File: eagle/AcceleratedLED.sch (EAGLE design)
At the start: 19 parts, among them Q1 16MHZ, U1 ATMEGA328, U8 TXB0108PWR

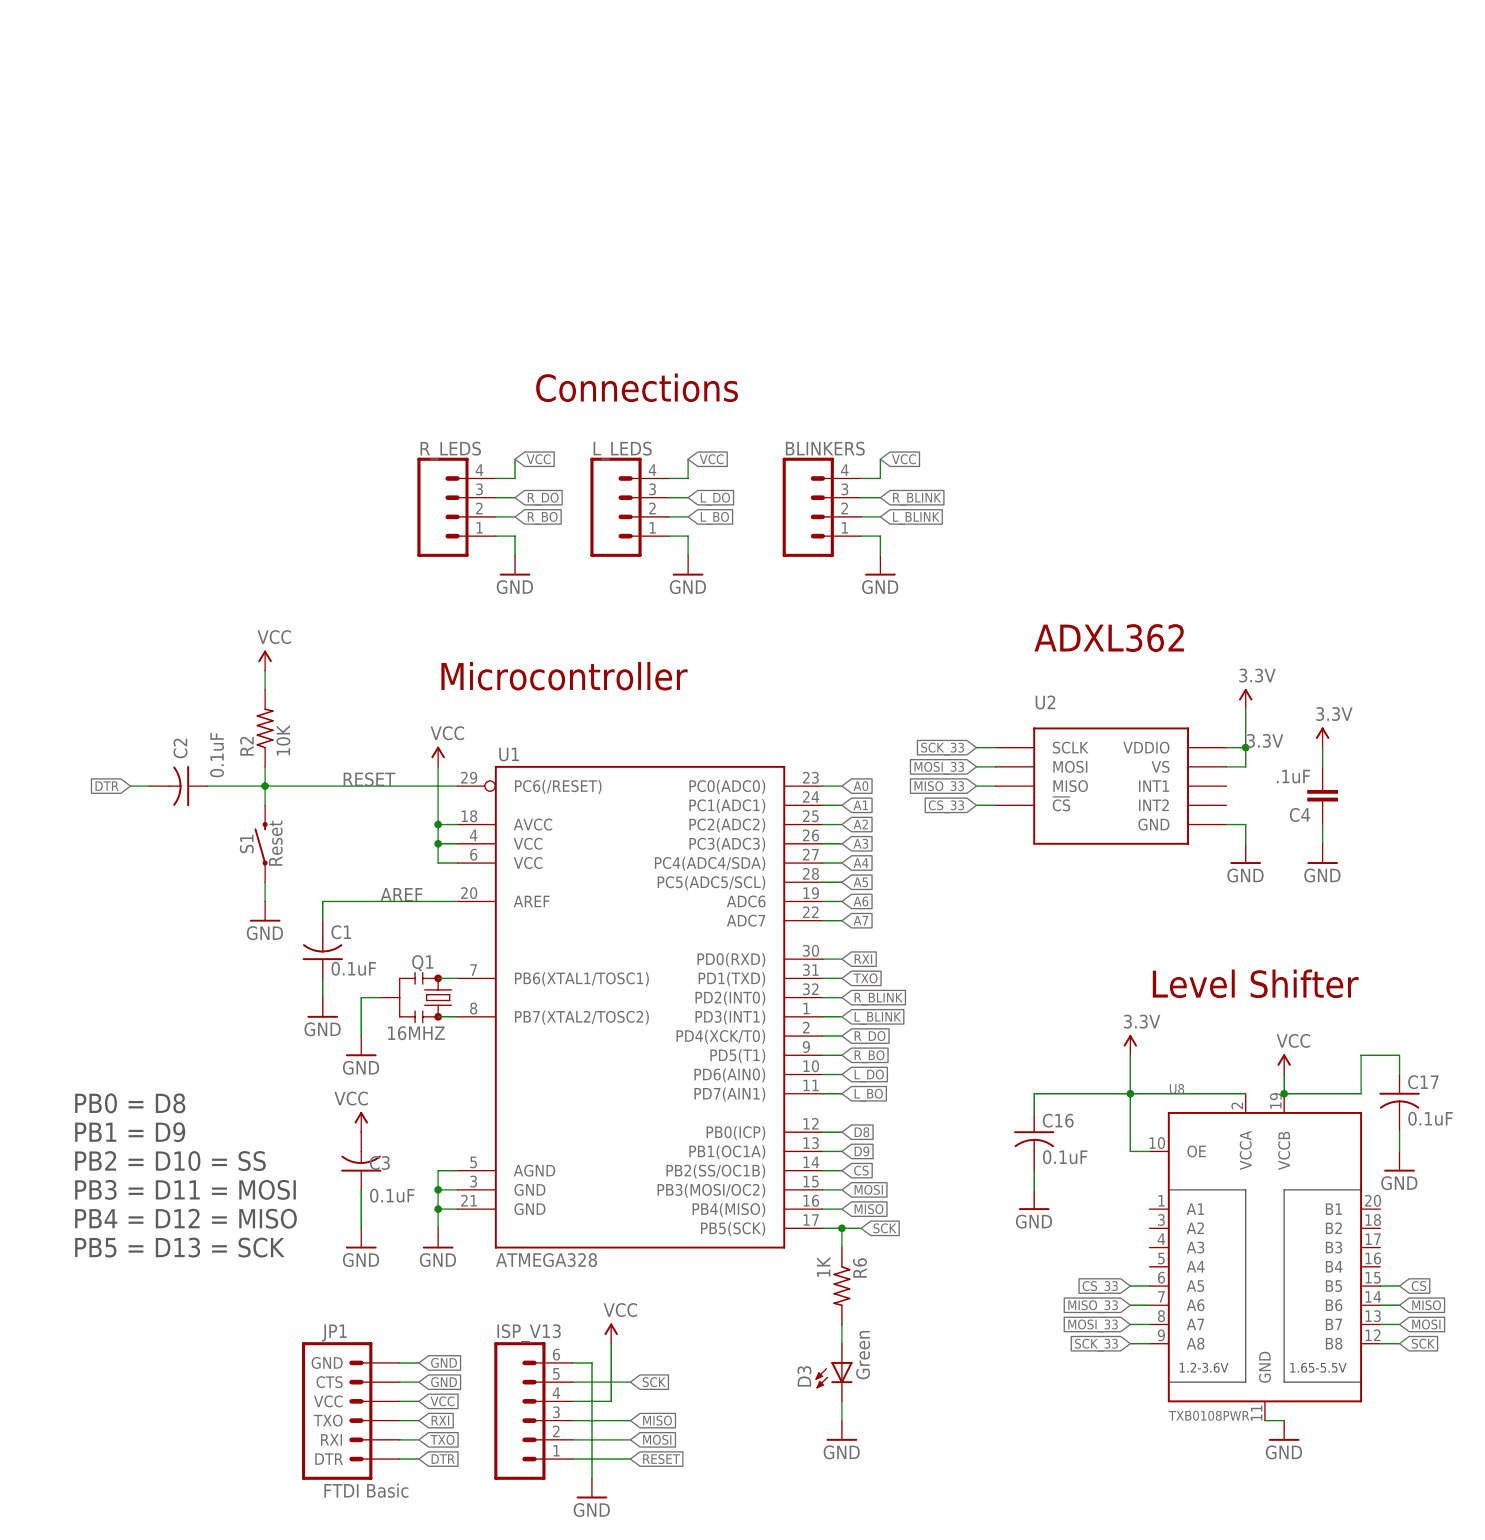
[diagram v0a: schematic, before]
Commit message: Add switching power
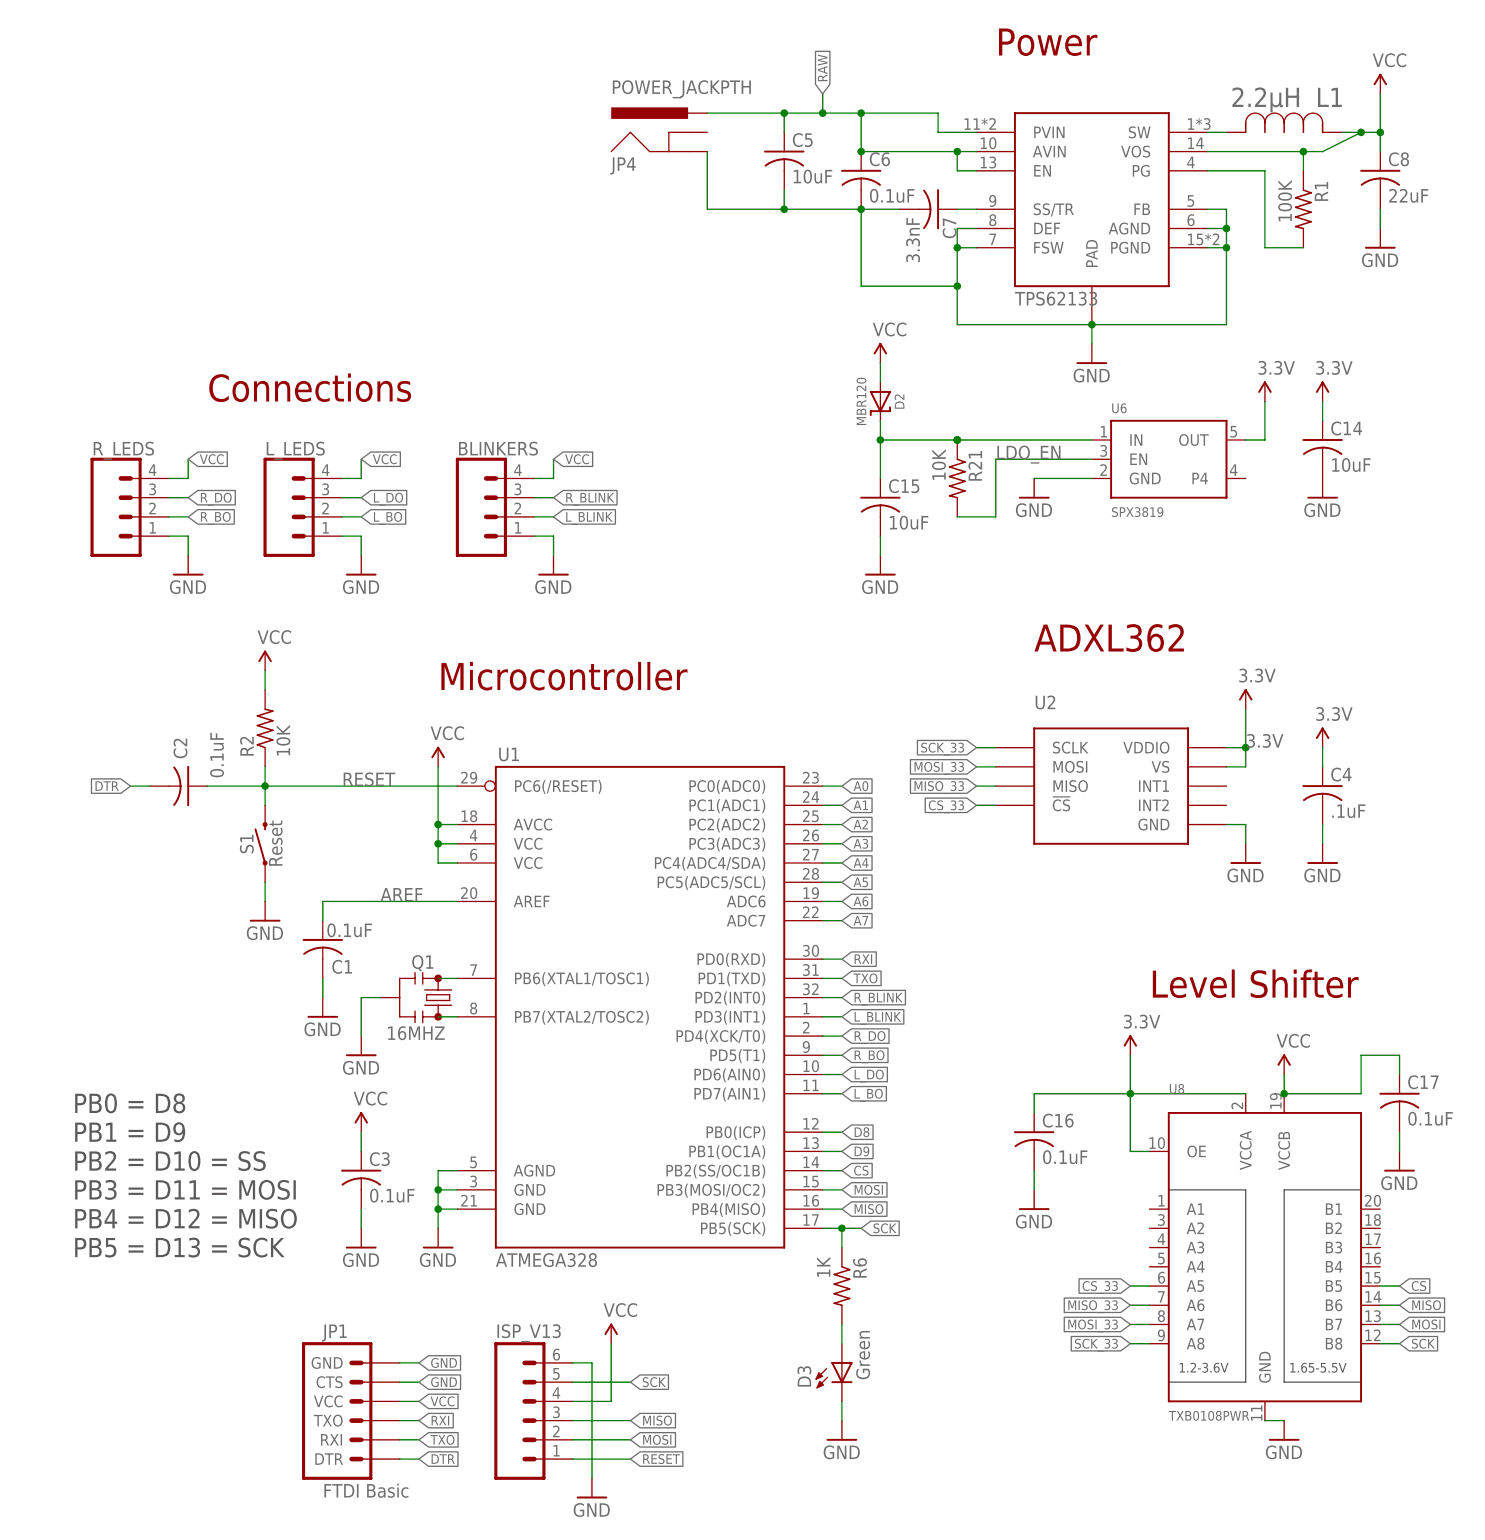
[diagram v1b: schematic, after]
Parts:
- added C14, C5: 10uF, RemoteMotion:C-USC0805
- added C15: 10uF, MotionSign:C-USC0805
- added C6: 0.1uF, MotionSign:C-USC0805
- added C7: 3.3nF, MotionSign:C-USC0805
- added C8: 22uF, RemoteMotion:C-USC0805
- added D2: MBR120, MotionSign:DIODE-SCHOTTKYSOD-123
- added IC1: TPS62133, robopoly:TPS62133
- added JP4: POWER_JACKPTH, MotionSign:POWER_JACKPTH
- added L1: 2.2μH, bg_eagle_lib:IHLP1212BZER2R2M11IND_IHLP-1212BZ-L
- added R1: 100K, MotionSign:R-US_M0805
- added R21: 10K, MotionSign:R-US_M0805
- added U6: SPX3819, MotionSign:VREG_SOT23-5
- C4: device SparkFun-Capacitors:0.1UF-25V(+80/-20%)(0603) -> RemoteMotion:C-USC0805; PROD_ID CAP-00810 -> (none)
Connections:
- new net LDO_EN: R21.2, U6.EN
- new net N$23: C15.1, D2.C, R21.1, U6.IN
- new net PG: IC1.PG, R1.2
- new net RAW: C5.1, C6.1, IC1.AVIN, IC1.EN, IC1.PVIN, JP4.PWR
- new net SS/TR: C7.1, IC1.SS/TR
- new net SW: IC1.SW, L1.2
- net 3.3V: now also C14.1, C4.1, U6.OUT; no longer C4.2
- net AREF: now also C1.1; no longer C1.2
- net GND: now also C1.2, C14.2, C15.2, C3.2, C4.2, C5.2, C6.2, C7.2, C8.2, IC1.AGND, IC1.DEF, IC1.FB, IC1.FSW, IC1.PAD, IC1.PGND, JP4.GND, U6.GND; no longer C1.1, C3.1, C4.1
- net VCC: now also C3.1, C8.1, D2.A, IC1.VOS, L1.1, R1.1; no longer C3.2
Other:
- note added: "Power"
- moved on the sheet: BLINKERS, C1, C3, L_LEDS, R_LEDS

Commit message: changes
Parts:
- BLINKERS: device MotionSign:CONN_04JST-PTH -> SparkFun-Connectors:M03JST-PTH
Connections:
- net L_BO renamed L_SCK
- net L_DO renamed L_DATA
- net R_BO renamed R_SCK
- net R_DO renamed R_DATA
- net VCC: no longer BLINKERS.4
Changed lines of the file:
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@@
 <setting verticaltext="up"/>
 </settings>
-<grid distance="0.1" unitdist="inch" unit="inch" style="lines" multiple="1" display="yes" altdistance="0.01" altunitdist="inch" altunit="inch"/>
+<grid distance="0.1" unitdist="inch" unit="inch" style="lines" multiple="1" display="no" altdistance="0.01" altunitdist="inch" altunit="inch"/>
 <layers>
 <layer number="1" name="Top" color="4" fill="1" visible="no" active="no"/>
@@
 <part name="L_LEDS" library="MotionSign" library_urn="urn:adsk.eagle:library:3048452" deviceset="CONN_04" device="JST-PTH" package3d_urn="urn:adsk.eagle:package:3048844/2"/>
 <part name="GND9" library="MotionSign" library_urn="urn:adsk.eagle:library:3048452" deviceset="GND" device=""/>
-<part name="BLINKERS" library="MotionSign" library_urn="urn:adsk.eagle:library:3048452" deviceset="CONN_04" device="JST-PTH" package3d_urn="urn:adsk.eagle:package:3048844/2"/>
 <part name="GND10" library="MotionSign" library_urn="urn:adsk.eagle:library:3048452" deviceset="GND" device=""/>
 <part name="C14" library="RemoteMotion" library_urn="urn:adsk.eagle:library:2810894" deviceset="C-US" device="C0805" package3d_urn="urn:adsk.eagle:package:2811338/2" value="10uF"/>
@@
 <part name="JP4" library="MotionSign" library_urn="urn:adsk.eagle:library:3048452" deviceset="POWER_JACK" device="PTH" package3d_urn="urn:adsk.eagle:package:3048907/2" value="POWER_JACKPTH"/>
 <part name="SUPPLY3" library="MotionSign" library_urn="urn:adsk.eagle:library:3048452" deviceset="VCC" device=""/>
+<part name="BLINKERS" library="SparkFun-Connectors" deviceset="M03" device="JST-PTH"/>
 </parts>
 <sheets>
@@
 <instance part="L_LEDS" gate="G$1" x="-15.24" y="129.54"/>
 <instance part="GND9" gate="1" x="-7.62" y="121.92"/>
-<instance part="BLINKERS" gate="G$1" x="10.16" y="129.54"/>
-<instance part="GND10" gate="1" x="17.78" y="121.92"/>
+<instance part="GND10" gate="1" x="17.78" y="149.86"/>
 <instance part="C14" gate="G$1" x="119.38" y="139.7"/>
 <instance part="U6" gate="G$1" x="99.06" y="137.16"/>
@@
 <instance part="JP4" gate="G$1" x="35.56" y="175.26"/>
 <instance part="SUPPLY3" gate="1" x="-7.62" y="48.26"/>
+<instance part="BLINKERS" gate="G$1" x="7.62" y="157.48"/>
 </instances>
 <busses>
@@
 <wire x1="-7.62" y1="127" x2="-7.62" y2="124.46" width="0.1524" layer="91"/>
 <pinref part="GND9" gate="1" pin="GND"/>
-</segment>
-<segment>
-<pinref part="BLINKERS" gate="G$1" pin="1"/>
-<wire x1="15.24" y1="127" x2="17.78" y2="127" width="0.1524" layer="91"/>
-<wire x1="17.78" y1="127" x2="17.78" y2="124.46" width="0.1524" layer="91"/>
-<pinref part="GND10" gate="1" pin="GND"/>
 </segment>
 <segment>
@@
 <wire x1="127" y1="167.64" x2="127" y2="170.18" width="0.1524" layer="91"/>
 </segment>
+<segment>
+<pinref part="BLINKERS" gate="G$1" pin="1"/>
+<wire x1="15.24" y1="154.94" x2="17.78" y2="154.94" width="0.1524" layer="91"/>
+<pinref part="GND10" gate="1" pin="GND"/>
+<wire x1="17.78" y1="152.4" x2="17.78" y2="154.94" width="0.1524" layer="91"/>
+</segment>
 </net>
 <net name="AREF" class="0">
@@
 <wire x1="-7.62" y1="134.62" x2="-7.62" y2="137.16" width="0.1524" layer="91"/>
 <label x="-7.62" y="137.16" size="1.27" layer="95" xref="yes"/>
-</segment>
-<segment>
-<pinref part="BLINKERS" gate="G$1" pin="4"/>
-<wire x1="15.24" y1="134.62" x2="17.78" y2="134.62" width="0.1524" layer="91"/>
-<wire x1="17.78" y1="134.62" x2="17.78" y2="137.16" width="0.1524" layer="91"/>
-<label x="17.78" y="137.16" size="1.27" layer="95" xref="yes"/>
 </segment>
 <segment>
@@
 </segment>
 </net>
-<net name="R_BO" class="0">
-<segment>
-<wire x1="53.34" y1="58.42" x2="55.88" y2="58.42" width="0.1524" layer="91"/>
-<pinref part="U1" gate="G$1" pin="PD5(T1)"/>
-<label x="55.88" y="58.42" size="1.27" layer="95" xref="yes"/>
-</segment>
-<segment>
-<pinref part="R_LEDS" gate="G$1" pin="2"/>
-<wire x1="-33.02" y1="129.54" x2="-30.48" y2="129.54" width="0.1524" layer="91"/>
-<label x="-30.48" y="129.54" size="1.27" layer="95" xref="yes"/>
-</segment>
-</net>
 <net name="3.3V" class="0">
 <segment>
@@
 <net name="R_BLINK" class="0">
 <segment>
-<pinref part="BLINKERS" gate="G$1" pin="3"/>
-<wire x1="15.24" y1="132.08" x2="17.78" y2="132.08" width="0.1524" layer="91"/>
-<label x="17.78" y="132.08" size="1.27" layer="95" xref="yes"/>
-</segment>
-<segment>
 <pinref part="U1" gate="G$1" pin="PD2(INT0)"/>
 <wire x1="53.34" y1="66.04" x2="55.88" y2="66.04" width="0.1524" layer="91"/>
 <label x="55.88" y="66.04" size="1.27" layer="95" xref="yes"/>
 </segment>
+<segment>
+<pinref part="BLINKERS" gate="G$1" pin="3"/>
+<wire x1="15.24" y1="160.02" x2="17.78" y2="160.02" width="0.1524" layer="91"/>
+<label x="17.78" y="160.02" size="1.27" layer="95" xref="yes"/>
+</segment>
 </net>
 <net name="L_BLINK" class="0">
-<segment>
-<pinref part="BLINKERS" gate="G$1" pin="2"/>
-<wire x1="15.24" y1="129.54" x2="17.78" y2="129.54" width="0.1524" layer="91"/>
-<label x="17.78" y="129.54" size="1.27" layer="95" xref="yes"/>
-</segment>
 <segment>
 <pinref part="U1" gate="G$1" pin="PD3(INT1)"/>
@@
 <label x="55.88" y="63.5" size="1.27" layer="95" xref="yes"/>
 </segment>
-</net>
-<net name="L_DO" class="0">
+<segment>
+<pinref part="BLINKERS" gate="G$1" pin="2"/>
+<wire x1="15.24" y1="157.48" x2="17.78" y2="157.48" width="0.1524" layer="91"/>
+<label x="17.78" y="157.48" size="1.27" layer="95" xref="yes"/>
+</segment>
+</net>
+<net name="L_DATA" class="0">
 <segment>
 <pinref part="L_LEDS" gate="G$1" pin="3"/>
@@
 </segment>
 </net>
-<net name="L_BO" class="0">
+<net name="L_SCK" class="0">
 <segment>
 <pinref part="L_LEDS" gate="G$1" pin="2"/>
@@
 </segment>
 </net>
-<net name="R_DO" class="0">
+<net name="R_DATA" class="0">
 <segment>
 <pinref part="R_LEDS" gate="G$1" pin="3"/>
@@
 </segment>
 </net>
+<net name="R_SCK" class="0">
+<segment>
+<wire x1="53.34" y1="58.42" x2="55.88" y2="58.42" width="0.1524" layer="91"/>
+<pinref part="U1" gate="G$1" pin="PD5(T1)"/>
+<label x="55.88" y="58.42" size="1.27" layer="95" xref="yes"/>
+</segment>
+<segment>
+<pinref part="R_LEDS" gate="G$1" pin="2"/>
+<wire x1="-33.02" y1="129.54" x2="-30.48" y2="129.54" width="0.1524" layer="91"/>
+<label x="-30.48" y="129.54" size="1.27" layer="95" xref="yes"/>
+</segment>
+</net>

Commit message: small board changes
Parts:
- added EFFECT_LEDS: (no value), MotionSign:CONN_04JST-PTH
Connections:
- removed net D8: U1.PB0(ICP)
- removed net D9: U1.PB1(OC1A)
- new net E_DATA: EFFECT_LEDS.3, U1.PB0(ICP)
- new net E_SCK: EFFECT_LEDS.2, U1.PB1(OC1A)
- net GND: now also EFFECT_LEDS.1
- net VCC: now also EFFECT_LEDS.4
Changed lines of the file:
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@@
 <part name="SUPPLY3" library="MotionSign" library_urn="urn:adsk.eagle:library:3048452" deviceset="VCC" device=""/>
 <part name="BLINKERS" library="SparkFun-Connectors" deviceset="M03" device="JST-PTH"/>
+<part name="EFFECT_LEDS" library="MotionSign" library_urn="urn:adsk.eagle:library:3048452" deviceset="CONN_04" device="JST-PTH" package3d_urn="urn:adsk.eagle:package:3048844/2"/>
+<part name="GND11" library="MotionSign" library_urn="urn:adsk.eagle:library:3048452" deviceset="GND" device=""/>
 </parts>
 <sheets>
@@
 <instance part="SUPPLY3" gate="1" x="-7.62" y="48.26"/>
 <instance part="BLINKERS" gate="G$1" x="7.62" y="157.48"/>
+<instance part="EFFECT_LEDS" gate="G$1" x="10.16" y="129.54"/>
+<instance part="GND11" gate="1" x="17.78" y="121.92"/>
 </instances>
 <busses>
@@
 <wire x1="17.78" y1="152.4" x2="17.78" y2="154.94" width="0.1524" layer="91"/>
 </segment>
+<segment>
+<pinref part="EFFECT_LEDS" gate="G$1" pin="1"/>
+<wire x1="15.24" y1="127" x2="17.78" y2="127" width="0.1524" layer="91"/>
+<wire x1="17.78" y1="127" x2="17.78" y2="124.46" width="0.1524" layer="91"/>
+<pinref part="GND11" gate="1" pin="GND"/>
+</segment>
 </net>
 <net name="AREF" class="0">
@@
 <wire x1="-7.62" y1="45.72" x2="-7.62" y2="48.26" width="0.1524" layer="91"/>
 </segment>
+<segment>
+<pinref part="EFFECT_LEDS" gate="G$1" pin="4"/>
+<wire x1="15.24" y1="134.62" x2="22.86" y2="134.62" width="0.1524" layer="91"/>
+<wire x1="22.86" y1="134.62" x2="22.86" y2="137.16" width="0.1524" layer="91"/>
+<label x="22.86" y="137.16" size="1.27" layer="95" xref="yes"/>
+</segment>
 </net>
 <net name="A5" class="0">
@@
 </segment>
 </net>
-<net name="D9" class="0">
-<segment>
-<wire x1="53.34" y1="45.72" x2="55.88" y2="45.72" width="0.1524" layer="91"/>
-<pinref part="U1" gate="G$1" pin="PB1(OC1A)"/>
-<label x="55.88" y="45.72" size="1.27" layer="95" xref="yes"/>
-</segment>
-</net>
 <net name="A1" class="0">
 <segment>
@@
 <pinref part="U1" gate="G$1" pin="PC1(ADC1)"/>
 <label x="55.88" y="91.44" size="1.27" layer="95" xref="yes"/>
-</segment>
-</net>
-<net name="D8" class="0">
-<segment>
-<pinref part="U1" gate="G$1" pin="PB0(ICP)"/>
-<wire x1="53.34" y1="48.26" x2="55.88" y2="48.26" width="0.1524" layer="91"/>
-<label x="55.88" y="48.26" size="1.27" layer="95" xref="yes"/>
 </segment>
 </net>
@@
 </segment>
 </net>
+<net name="E_DATA" class="0">
+<segment>
+<pinref part="EFFECT_LEDS" gate="G$1" pin="3"/>
+<wire x1="15.24" y1="132.08" x2="17.78" y2="132.08" width="0.1524" layer="91"/>
+<label x="17.78" y="132.08" size="1.27" layer="95" xref="yes"/>
+</segment>
+<segment>
+<pinref part="U1" gate="G$1" pin="PB0(ICP)"/>
+<wire x1="53.34" y1="48.26" x2="55.88" y2="48.26" width="0.1524" layer="91"/>
+<label x="55.88" y="48.26" size="1.27" layer="95" xref="yes"/>
+</segment>
+</net>
+<net name="E_SCK" class="0">
+<segment>
+<pinref part="EFFECT_LEDS" gate="G$1" pin="2"/>
+<wire x1="15.24" y1="129.54" x2="17.78" y2="129.54" width="0.1524" layer="91"/>
+<label x="17.78" y="129.54" size="1.27" layer="95" xref="yes"/>
+</segment>
+<segment>
+<wire x1="53.34" y1="45.72" x2="55.88" y2="45.72" width="0.1524" layer="91"/>
+<pinref part="U1" gate="G$1" pin="PB1(OC1A)"/>
+<label x="55.88" y="45.72" size="1.27" layer="95" xref="yes"/>
+</segment>
+</net>
